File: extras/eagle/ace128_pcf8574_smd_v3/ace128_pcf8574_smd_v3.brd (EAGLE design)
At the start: 30.5 x 30.5 mm, 17 parts, among them IC1 24AA00OT, J1 GROVE I2C, U1 PCF8574T

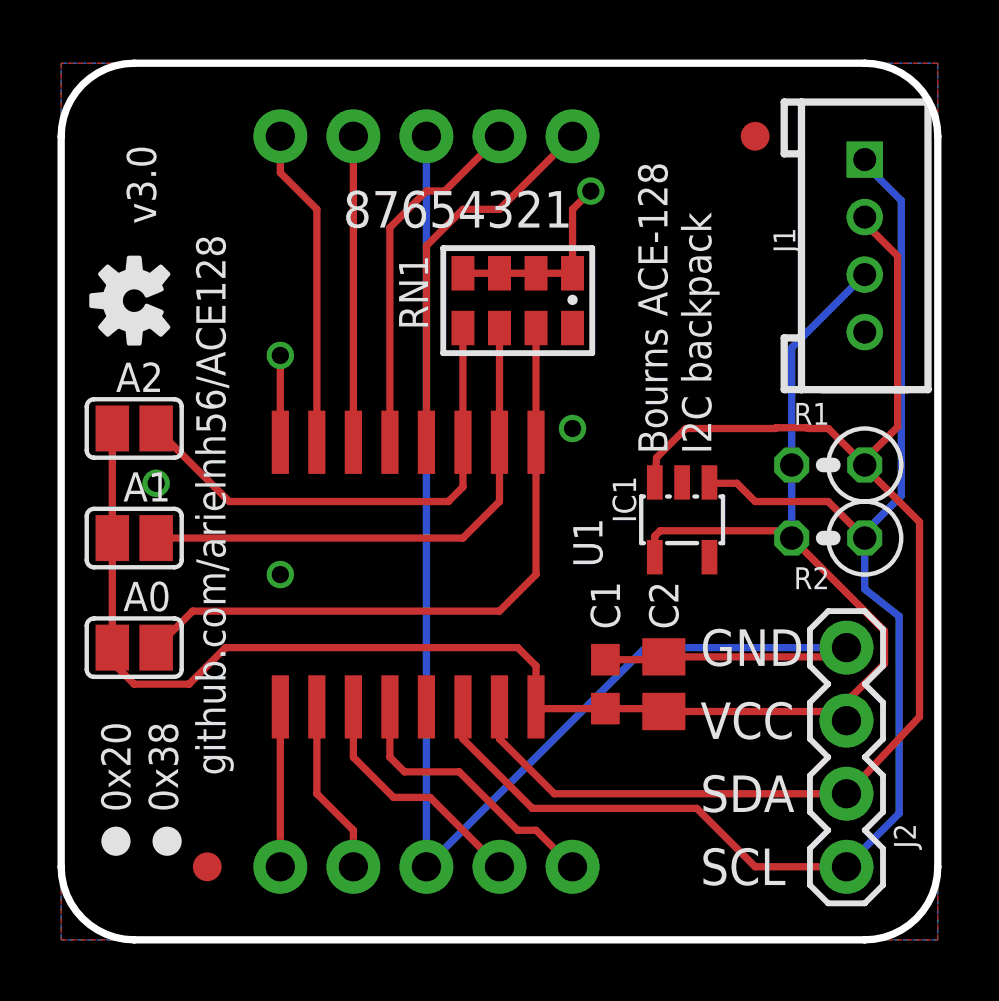
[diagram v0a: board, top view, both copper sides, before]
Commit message: v3.1
Moved the fiducials - one of them as being confused with the silkskreen version dots.
Update version to 3.1
Going to production with this.
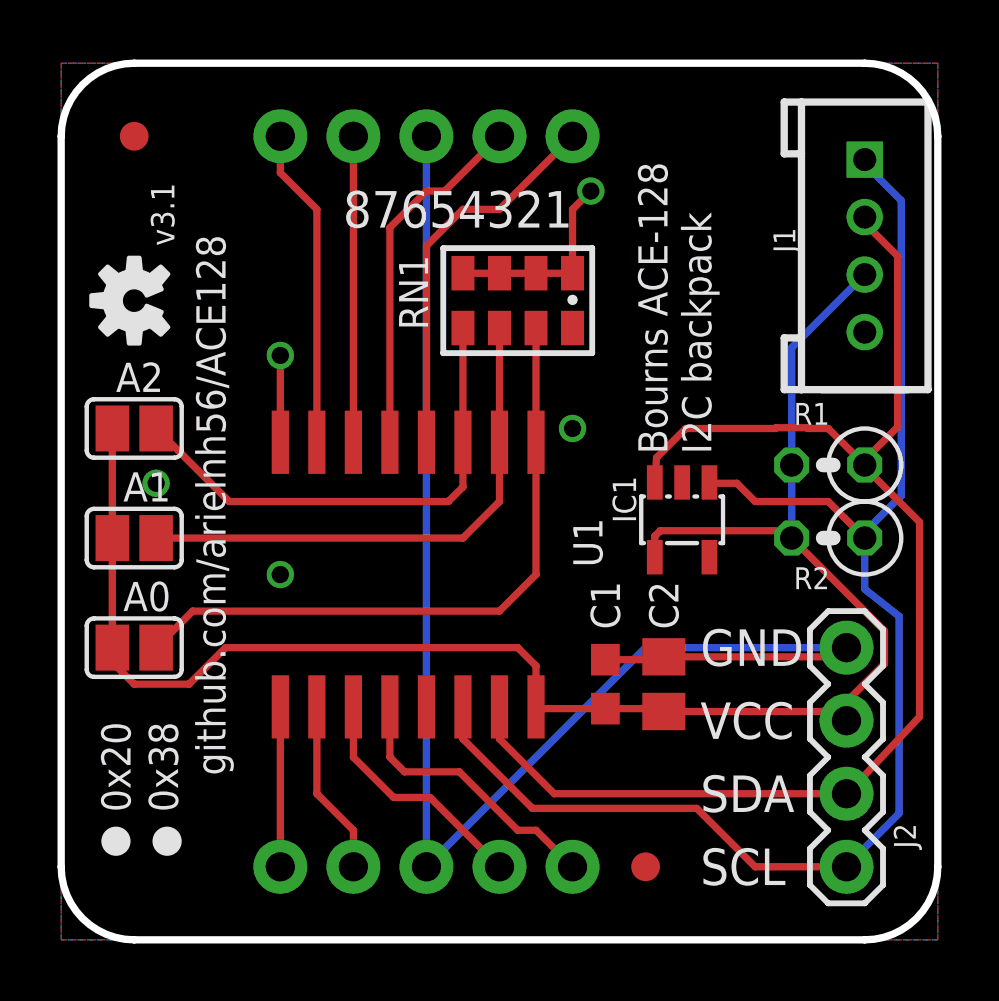
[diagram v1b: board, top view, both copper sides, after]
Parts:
- moved FD2 25.7 mm to (20.3, 2.54)
- moved FD1 25.5 mm to (2.54, 27.9)
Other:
- board text added: "v3.1"
- board text removed: "v3.0"
